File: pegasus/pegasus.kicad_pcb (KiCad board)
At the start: 2 copper layers, 39 x 98 mm, 24 parts, among them IC2 RFD900ux-SMT, IC3 L70B-M39, J1 Screw_Terminal_01x04, J2 Screw_Terminal_01x02, Q1 ST3413A, U1 Teensy4.0, U2 CON-SMA-EDGE-S, U3 CON-SMA-EDGE-S, U4 XTSD04GCLGEGA, U5 AZ1117-ADJ

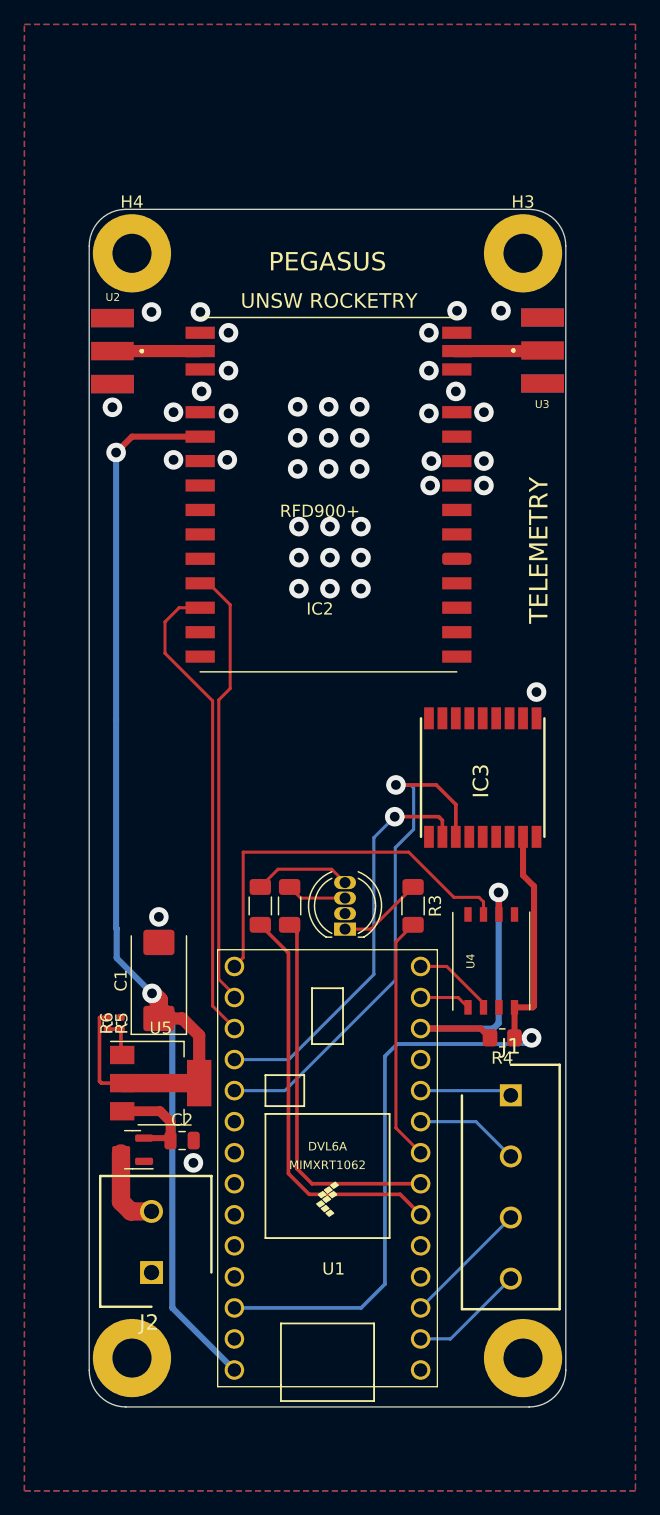
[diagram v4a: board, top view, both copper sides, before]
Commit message: reposition GPS to center of board, add gps reset circuitry
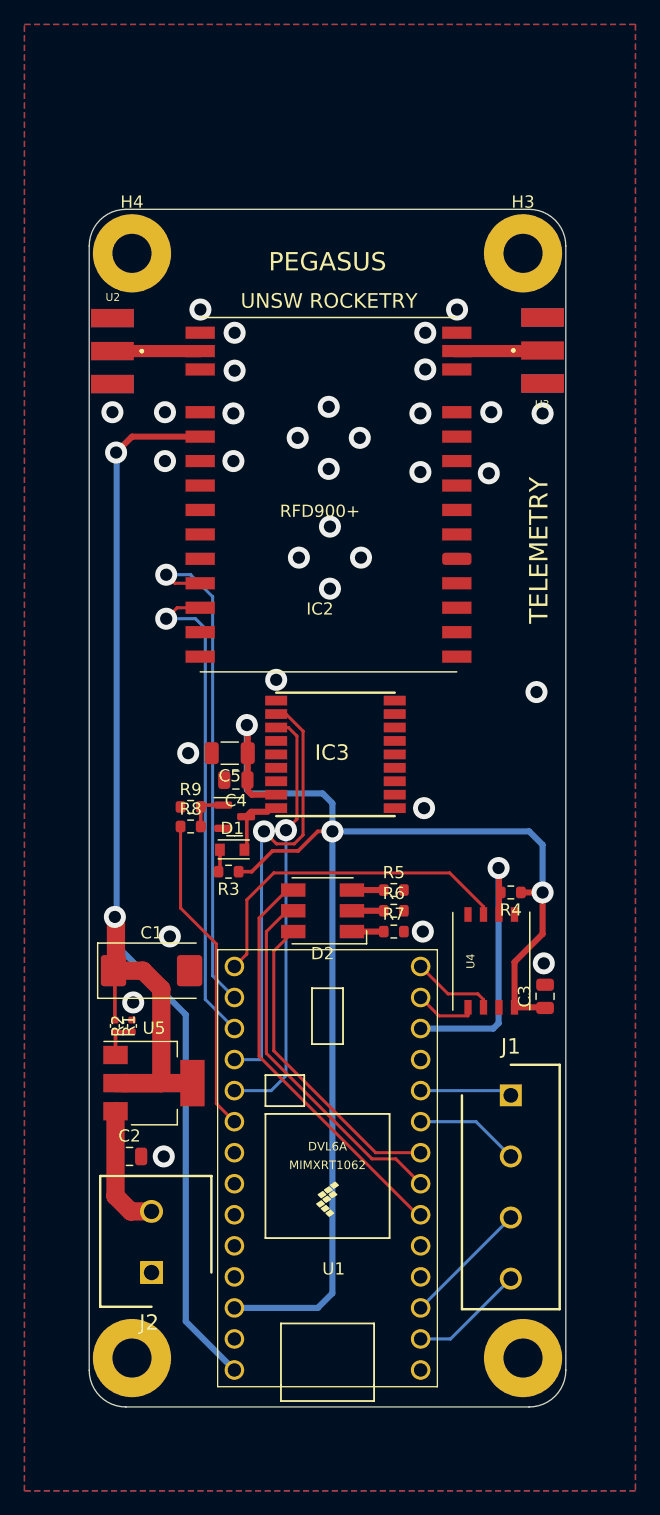
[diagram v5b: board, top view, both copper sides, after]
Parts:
- added C3: 100nF, Capacitor_SMD:C_0805_2012Metric, F.Cu at (123.3, 126.4)
- added C4: 100nF, Capacitor_SMD:C_0805_2012Metric, F.Cu at (98.0, 108.7)
- added C5: 4.7uF, Capacitor_SMD:C_1206_3216Metric, F.Cu at (97.5, 106.5)
- added D2: LED_RGB, LED_SMD:LED_RGB_5050-6, F.Cu at (105.1, 119.4)
- added R7: 4R, Resistor_SMD:R_0603_1608Metric, F.Cu at (110.9, 121.1)
- added R8: 10k, Resistor_SMD:R_0603_1608Metric, F.Cu at (94.3, 112.5)
- added R9: 10k, Resistor_SMD:R_0603_1608Metric, F.Cu at (94.3, 110.9)
- C2: value C -> 10uF
- D1: value RGB LED -> LED; footprint LED_THT:LED_D5.0mm-4_RGB -> LED_SMD:LED_miniPLCC_2315
- Q1: value ST3413A -> BC817
- R1: value 220 -> 50R; footprint Resistor_SMD:R_1206_3216Metric_Pad1.30x1.75mm_HandSolder -> Capacitor_SMD:C_0402_1005Metric
- R2: value 220 -> 150R; footprint Resistor_SMD:R_1206_3216Metric_Pad1.30x1.75mm_HandSolder -> Capacitor_SMD:C_0402_1005Metric
- R3: value 220 -> 3.0k; footprint Resistor_SMD:R_1206_3216Metric_Pad1.30x1.75mm_HandSolder -> Resistor_SMD:R_0603_1608Metric
- R4: footprint Resistor_SMD:R_0805_2012Metric_Pad1.20x1.40mm_HandSolder -> Resistor_SMD:R_0603_1608Metric
- R5: value 50R -> 65R; footprint Capacitor_SMD:C_0402_1005Metric -> Resistor_SMD:R_0603_1608Metric
- R6: value 150R -> 4R; footprint Capacitor_SMD:C_0402_1005Metric -> Resistor_SMD:R_0603_1608Metric
- moved Q1 28.5 mm to (97.9, 111.7), turned to 0 degrees
- moved R5 25.8 mm to (110.9, 117.7), turned to 0 degrees
- moved R6 24.1 mm to (110.9, 119.4), turned to 0 degrees
- moved R1 17.3 mm to (88.1, 128.8)
- moved R3 15.4 mm to (97.4, 116.2), turned to 180 degrees
- moved R2 14.4 mm to (89.5, 128.8), turned to 90 degrees
- moved IC3 12.2 mm to (106.1, 106.6), turned to 0 degrees
- moved R4 11.9 mm to (120.5, 117.9)
- moved D1 11.3 mm to (97.7, 114.4), turned to 180 degrees
- moved C2 4.49 mm to (89.3, 139.5)
- moved C1 1.00 mm to (91.1, 124.3), turned to 0 degrees
- moved U5 0.55 mm to (91.3, 133.5)
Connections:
- C2 pad 1: Net-(Q1-Pad2) -> Net-(C2-Pad1)
- D1 pad 2: GND -> Net-(D1-Pad2)
- IC3 pad 9: unconnected-(IC3-Pad9) -> Net-(D1-Pad1)
- J2 pad 2: Net-(J2-Pad2) -> Net-(C2-Pad1)
- Q1 pad 1: GND -> Net-(Q1-Pad1)
- Q1 pad 2: Net-(Q1-Pad2) -> GND
- Q1 pad 3: Net-(J2-Pad2) -> Net-(D1-Pad1)
- R1 pad 1: Net-(D1-Pad3) -> +5V
- R1 pad 2: RGB2 -> Net-(R1-Pad2)
- R2 pad 1: Net-(D1-Pad4) -> Net-(R1-Pad2)
- R2 pad 2: RGB1 -> GND
- R3 pad 1: Net-(D1-Pad1) -> +3V3
- R3 pad 2: RGB3 -> Net-(D1-Pad2)
- R5 pad 1: +5V -> Net-(D2-Pad3)
- R5 pad 2: Net-(R5-Pad2) -> GND
- R6 pad 1: Net-(R5-Pad2) -> Net-(D2-Pad2)
- U1 pad 25: unconnected-(U1-Pad25) -> GPS_~{RESET}
- U1 pad 6: RGB1 -> LED_{BLUE}
- U1 pad 7: RGB2 -> LED_{GREEN
- U1 pad 8: RGB3 -> LED_{RED}
- U5 pad 1: Net-(R5-Pad2) -> Net-(R1-Pad2)
- U5 pad 3: Net-(Q1-Pad2) -> Net-(C2-Pad1)
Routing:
- net +3V3: track 64.2 -> 114.5 mm, vias 1 -> 3
- net LED_{BLUE}: track 0.00 -> 33.6 mm
- net RGB1: track 33.5 -> 0.00 mm
- net RGB2: track 30.8 -> 0.00 mm
- net LED_{GREEN: track 0.00 -> 29.9 mm
- net GPS_~{RESET}: track 0.00 -> 26.0 mm
- net LED_{RED}: track 0.00 -> 25.9 mm
- net RGB3: track 20.1 -> 0.00 mm
- net Net-(C2-Pad1): track 0.00 -> 10.4 mm
- net TX4: track 43.0 -> 34.9 mm
- net Net-(Q1-Pad2): track 8.10 -> 0.00 mm
- net Net-(D1-Pad4): track 7.99 -> 0.00 mm
- net Net-(J2-Pad2): track 6.78 -> 0.00 mm
- net +5V: track 110.6 -> 116.8 mm
- net TX3: track 36.2 -> 41.1 mm, vias 0 -> 1
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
